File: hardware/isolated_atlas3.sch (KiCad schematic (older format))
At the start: 15 parts, among them J501 CONN_01X02, P5 ATLAS_DO_PROBE, U501 ADM3260, U502 ATLAS_DO

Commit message: Upgrade to Kicad 5.
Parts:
- C501, C502, C503, C504, C505, C506: symbol C -> fk-atlas-rescue:C
- J501: symbol CONN_01X02 -> fk-atlas-rescue:CONN_01X02
- P5: symbol WATER_PROBE -> fk-atlas-rescue:WATER_PROBE
- R501, R502, R503, R504, R505: symbol R -> fk-atlas-rescue:R
- U501: symbol adm3260 -> fk-atlas-rescue:adm3260
- U502: symbol ATLAS_SENSOR -> conservify:ATLAS_SENSOR
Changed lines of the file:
@@
-EESchema Schematic File Version 2
-LIBS:conservify
+EESchema Schematic File Version 4
 LIBS:fk-atlas-cache
-EELAYER 25 0
+EELAYER 26 0
 EELAYER END
 $Descr A4 11693 8268
@@
 $EndDescr
 $Comp
-L adm3260 U501
+L fk-atlas-rescue:adm3260 U501
 U 1 1 594C2CF0
 P 4400 2900
@@
 $EndComp
 $Comp
-L C C503
+L fk-atlas-rescue:C C503
 U 1 1 594C2CF5
 P 5650 3800
@@
 $EndComp
 $Comp
-L C C504
+L fk-atlas-rescue:C C504
 U 1 1 594C2CF9
 P 5650 4100
@@
 $EndComp
 $Comp
-L C C505
+L fk-atlas-rescue:C C505
 U 1 1 594C2CFC
 P 5650 4400
@@
 $EndComp
 $Comp
-L C C506
+L fk-atlas-rescue:C C506
 U 1 1 594C2D00
 P 5650 4650
@@
 $EndComp
 $Comp
-L C C501
+L fk-atlas-rescue:C C501
 U 1 1 5948D5F5
 P 2900 3800
@@
 $EndComp
 $Comp
-L C C502
+L fk-atlas-rescue:C C502
 U 1 1 5948D68D
 P 2900 4100
@@
 $EndComp
 $Comp
-L R R501
+L fk-atlas-rescue:R R501
 U 1 1 594C2D0D
 P 5650 3300
@@
 $EndComp
 $Comp
-L R R502
+L fk-atlas-rescue:R R502
 U 1 1 594C2D11
 P 6250 2700
@@
 $EndComp
 $Comp
-L R R504
+L fk-atlas-rescue:R R504
 U 1 1 594C2D15
 P 6700 2700
@@
 $EndComp
 $Comp
-L R R503
+L fk-atlas-rescue:R R503
 U 1 1 594C2D19
 P 6300 3250
@@
 $EndComp
 $Comp
-L R R505
+L fk-atlas-rescue:R R505
 U 1 1 594C2D1D
 P 6800 3250
@@
 $EndComp
 $Comp
-L VCC #PWR063
+L fk-atlas-rescue:VCC #PWR063
 U 1 1 5948EDC0
 P 2450 3750
@@
 $EndComp
 $Comp
-L VCC #PWR064
+L fk-atlas-rescue:VCC #PWR064
 U 1 1 5948EDF6
 P 2450 2350
@@
 $EndComp
 $Comp
-L ATLAS_SENSOR U502
+L conservify:ATLAS_SENSOR U502
 U 1 1 594C2D34
 P 8550 2900
@@
 $EndComp
 $Comp
-L CONN_01X02 J501
+L fk-atlas-rescue:CONN_01X02 J501
 U 1 1 594D403D
 P 10050 2950
@@
 $EndComp
 $Comp
-L WATER_PROBE P5
+L fk-atlas-rescue:WATER_PROBE P5
 U 1 1 59D2A6F4
 P 8800 3600

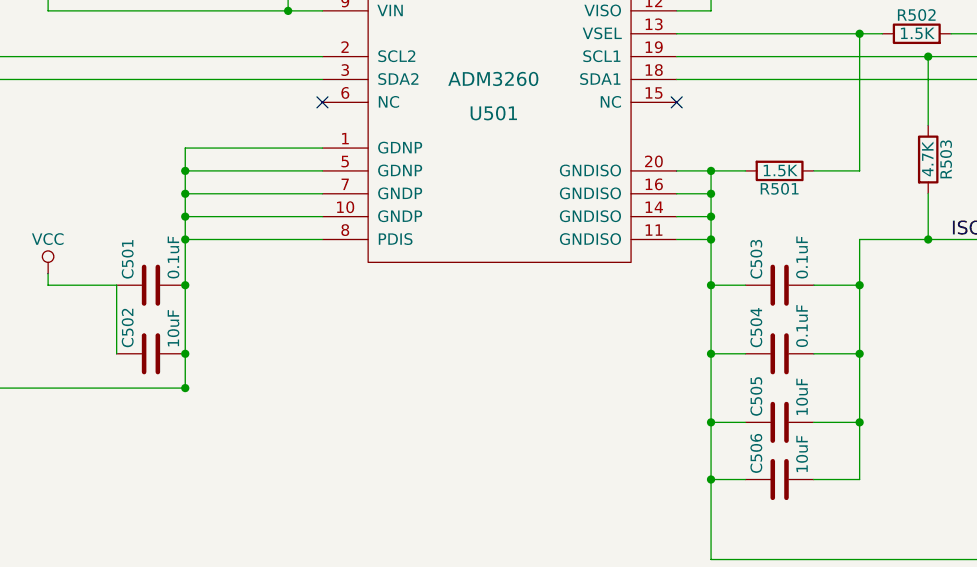
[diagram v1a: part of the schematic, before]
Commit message: Consistent part values across our schematics.
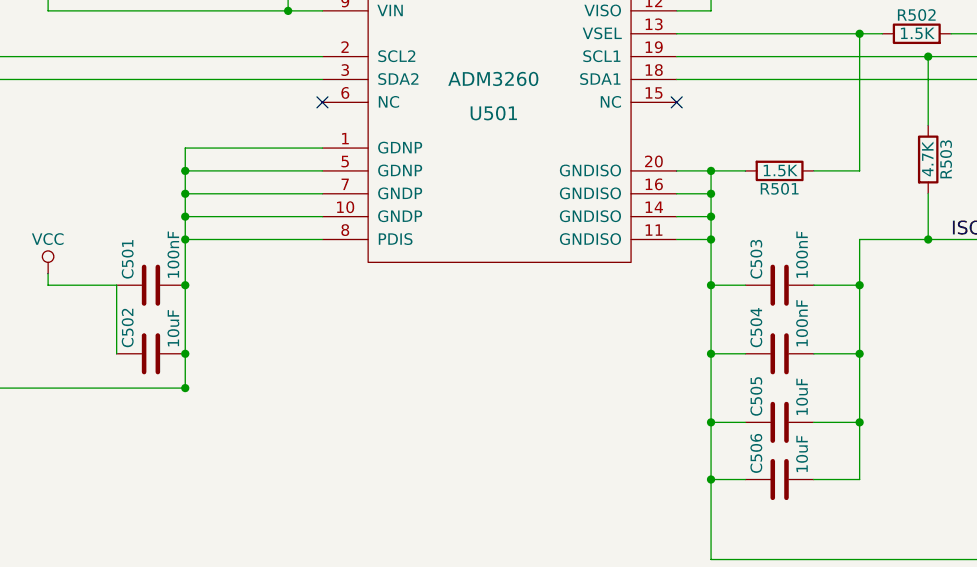
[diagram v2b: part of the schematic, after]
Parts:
- C501, C503, C504: value 0.1uF -> 100nF

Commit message: Part updates.
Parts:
- C501, C503, C504: Critical (none) -> (none); MFN (none) -> Murata Electronics; MFP (none) -> GRM188R71H104KA93D; Notes (none) -> (none); Package (none) -> (none); Source (none) -> ANY; Subsystem (none) -> (none); Supplier1 (none) -> mouser
- C502, C505, C506: Critical (none) -> (none); MFN (none) -> Taiyo Yuden; MFP (none) -> LMK107BBJ106KALT; Notes (none) -> (none); Package (none) -> (none); Source (none) -> ANY; Subsystem (none) -> (none); Supplier1 (none) -> mouser; spn1 81-GRM188R60J106ME47 -> 963-LMK107BBJ106KALT
- J501: Critical (none) -> (none); MFN (none) -> Amphenol RF; MFP (none) -> 031-5431; Notes (none) -> (none); Package (none) -> (none); Source (none) -> ANY; Subsystem (none) -> (none); Supplier1 (none) -> mouser
- P5: Critical (none) -> (none); MFN (none) -> (none); MFP (none) -> (none); Notes (none) -> (none); Package (none) -> (none); SPN1 (none) -> (none); Source (none) -> ANY; Subsystem (none) -> (none); Supplier1 (none) -> (none)
- R501, R502, R504: Critical (none) -> (none); MFN (none) -> (none); MFP (none) -> (none); Notes (none) -> (none); Package (none) -> (none); Source (none) -> ANY; Subsystem (none) -> (none); Supplier1 (none) -> (none)
- R503, R505: Critical (none) -> (none); MFN (none) -> Yageo; MFP (none) -> AF0603JR-074K7L; Notes (none) -> (none); Package (none) -> (none); Source (none) -> ANY; Subsystem (none) -> (none); Supplier1 (none) -> mouser
- U501: Critical (none) -> (none); MFN (none) -> Analog Devices / Linear Technology; MFP (none) -> ADM3260ARSZ; Notes (none) -> (none); Package (none) -> (none); Source (none) -> ANY; Subsystem (none) -> (none); Supplier1 (none) -> mouser
- U502: Critical (none) -> (none); MFN (none) -> (none); MFP (none) -> (none); Notes (none) -> (none); Package (none) -> (none); SPN1 (none) -> (none); Source (none) -> ANY; Subsystem (none) -> (none); Supplier1 (none) -> atlas

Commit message: Fix DRC in schematic mode.
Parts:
- C501, C502, C503, C504, C505, C506: symbol fk-atlas-rescue:C -> conservify:CAPACITOR_CERAMIC
- J501: symbol fk-atlas-rescue:CONN_01X02 -> conservify:CONN_01x02
- P5: symbol fk-atlas-rescue:WATER_PROBE -> conservify:ATLAS_WATER_PROBE
- R501, R502, R503, R504, R505: symbol fk-atlas-rescue:R -> conservify:R
- U501: symbol fk-atlas-rescue:adm3260 -> conservify:ADM3260
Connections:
- wire segments 52 -> 78
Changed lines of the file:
@@
 $EndDescr
 $Comp
-L fk-atlas-rescue:adm3260 U501
+L conservify:ADM3260 U501
 U 1 1 594C2CF0
 P 4400 2900
@@
 $EndComp
 $Comp
-L fk-atlas-rescue:C C503
+L conservify:CAPACITOR_CERAMIC C503
 U 1 1 594C2CF5
 P 5650 3800
@@
 $EndComp
 $Comp
-L fk-atlas-rescue:C C504
+L conservify:CAPACITOR_CERAMIC C504
 U 1 1 594C2CF9
 P 5650 4100
@@
 $EndComp
 $Comp
-L fk-atlas-rescue:C C505
+L conservify:CAPACITOR_CERAMIC C505
 U 1 1 594C2CFC
 P 5650 4400
@@
 $EndComp
 $Comp
-L fk-atlas-rescue:C C506
+L conservify:CAPACITOR_CERAMIC C506
 U 1 1 594C2D00
 P 5650 4650
@@
 $EndComp
 $Comp
-L fk-atlas-rescue:C C501
+L conservify:CAPACITOR_CERAMIC C501
 U 1 1 5948D5F5
 P 2900 3800
@@
 $EndComp
 $Comp
-L fk-atlas-rescue:C C502
+L conservify:CAPACITOR_CERAMIC C502
 U 1 1 5948D68D
 P 2900 4100
@@
 $EndComp
 $Comp
-L fk-atlas-rescue:R R501
+L conservify:R R501
 U 1 1 594C2D0D
 P 5650 3300
@@
 $EndComp
 $Comp
-L fk-atlas-rescue:R R502
+L conservify:R R502
 U 1 1 594C2D11
 P 6250 2700
@@
 $EndComp
 $Comp
-L fk-atlas-rescue:R R504
+L conservify:R R504
 U 1 1 594C2D15
 P 6700 2700
@@
 $EndComp
 $Comp
-L fk-atlas-rescue:R R503
+L conservify:R R503
 U 1 1 594C2D19
 P 6300 3250
@@
 $EndComp
 $Comp
-L fk-atlas-rescue:R R505
+L conservify:R R505
 U 1 1 594C2D1D
 P 6800 3250
@@
 $EndComp
 $Comp
-L fk-atlas-rescue:VCC #PWR063
+L conservify:VCC #PWR063
 U 1 1 5948EDC0
 P 2450 3750
@@
 $EndComp
 $Comp
-L fk-atlas-rescue:VCC #PWR064
+L conservify:VCC #PWR064
 U 1 1 5948EDF6
 P 2450 2350
@@
 $EndComp
 $Comp
-L fk-atlas-rescue:CONN_01X02 J501
+L conservify:CONN_01x02 J501
 U 1 1 594D403D
-P 10050 2950
-F 0 "J501" H 10050 3100 50  0000 C CNN
-F 1 "CONN_01X02" V 10150 2950 50  0000 C CNN
-F 2 "conservify:BNC" H 10050 2950 50  0001 C CNN
-F 3 "" H 10050 2950 50  0001 C CNN
-F 4 " " H 10050 3200 50  0001 C CNN "Critical"
-F 5 "Amphenol RF" H 10050 3200 50  0001 C CNN "MFN"
-F 6 "031-5431" H 10050 3200 50  0001 C CNN "MFP"
-F 7 " " H 10050 3200 50  0001 C CNN "Notes"
-F 8 " " H 10050 3200 50  0001 C CNN "Package"
-F 9 "ANY" H 10050 3200 50  0001 C CNN "Source"
-F 10 " " H 10050 3200 50  0001 C CNN "Subsystem"
-F 11 "mouser" H 10050 3200 50  0001 C CNN "Supplier1"
-F 12 "0" H 10050 3200 50  0001 C CNN "price"
-F 13 "523-31-5431" H 200 0   50  0001 C CNN "spn1"
-	1    10050 2950
-	1    0    0    -1
-$EndComp
-$Comp
-L fk-atlas-rescue:WATER_PROBE P5
+P 10050 2900
+F 0 "J501" H 10050 3050 50  0000 C CNN
+F 1 "CONN_01X02" V 10150 2900 50  0000 C CNN
+F 2 "conservify:BNC" H 10050 2900 50  0001 C CNN
+F 3 "" H 10050 2900 50  0001 C CNN
+F 4 " " H 10050 3150 50  0001 C CNN "Critical"
+F 5 "Amphenol RF" H 10050 3150 50  0001 C CNN "MFN"
+F 6 "031-5431" H 10050 3150 50  0001 C CNN "MFP"
+F 7 " " H 10050 3150 50  0001 C CNN "Notes"
+F 8 " " H 10050 3150 50  0001 C CNN "Package"
+F 9 "ANY" H 10050 3150 50  0001 C CNN "Source"
+F 10 " " H 10050 3150 50  0001 C CNN "Subsystem"
+F 11 "mouser" H 10050 3150 50  0001 C CNN "Supplier1"
+F 12 "0" H 10050 3150 50  0001 C CNN "price"
+F 13 "523-31-5431" H 200 -50 50  0001 C CNN "spn1"
+	1    10050 2900
+	1    0    0    -1
+$EndComp
+$Comp
+L conservify:ATLAS_WATER_PROBE P5
 U 1 1 59D2A6F4
 P 8800 3600
@@
 F 12 " " H 8800 3700 50  0001 C CNN "Supplier1"
 	1    8800 3600
+	1    0    0    -1
+$EndComp
+$Comp
+L conservify:PWR_FLAG #FLG0108
+U 1 1 5BCDA7BC
+P 7400 4900
+F 0 "#FLG0108" H 7400 4975 50  0001 C CNN
+F 1 "PWR_FLAG" H 7400 5050 50  0000 C CNN
+F 2 "" H 7400 4900 50  0001 C CNN
+F 3 "~" H 7400 4900 50  0001 C CNN
+	1    7400 4900
 	1    0    0    -1
 $EndComp
@@
 DO_PGND
 Wire Wire Line
-	5200 3300 5500 3300
-Wire Wire Line
-	5350 3300 5350 5000
+	5200 3300 5350 3300
+Wire Wire Line
+	5350 3300 5350 3400
 Wire Wire Line
 	5350 3600 5200 3600
@@
 	5800 3800 6000 3800
 Wire Wire Line
-	6000 3600 6000 4650
+	6000 3600 6000 3800
 Wire Wire Line
 	6000 4650 5800 4650
@@
 	5800 4100 6000 4100
 Wire Wire Line
-	5200 2800 7800 2800
-Wire Wire Line
-	5200 2900 7800 2900
-Wire Wire Line
-	5200 2700 6100 2700
+	5200 2800 6300 2800
+Wire Wire Line
+	5200 2900 6800 2900
+Wire Wire Line
+	5200 2700 6000 2700
 Wire Wire Line
 	6000 2700 6000 3300
@@
 	5350 2600 5350 2500
 Wire Wire Line
-	5200 2500 7400 2500
+	5200 2500 5350 2500
 Wire Wire Line
 	6900 2500 6900 2700
@@
 	6300 3400 6300 3600
 Wire Wire Line
-	6000 3600 6800 3600
+	6000 3600 6300 3600
 Wire Wire Line
 	6800 3600 6800 3400
 Wire Wire Line
-	2450 2600 3650 2600
-Wire Wire Line
-	2450 2350 2450 2600
+	2450 2600 3500 2600
+Wire Wire Line
+	2450 2350 2450 2450
 Wire Wire Line
 	3650 2500 3500 2500
@@
 	3650 3200 3050 3200
 Wire Wire Line
-	3050 3200 3050 4250
+	3050 3200 3050 3300
 Wire Wire Line
 	3050 4250 1750 4250
@@
 Wire Wire Line
 	9450 3000 9850 3000
+Wire Wire Line
+	7400 4900 7400 5000
+Wire Wire Line
+	5350 3500 5350 3600
+Wire Wire Line
+	5350 3400 5350 3500
+Wire Wire Line
+	5350 3600 5350 3800
+Wire Wire Line
+	5350 4400 5350 4650
+Wire Wire Line
+	5350 4100 5350 4400
+Wire Wire Line
+	5350 3800 5350 4100
+Wire Wire Line
+	6000 4400 6000 4650
+Wire Wire Line
+	6000 4100 6000 4400
+Wire Wire Line
+	5350 3300 5500 3300
+Wire Wire Line
+	5350 2500 6900 2500
+Wire Wire Line
+	6000 2700 6100 2700
+Wire Wire Line
+	6300 2800 7800 2800
+Wire Wire Line
+	6800 2900 7800 2900
+Wire Wire Line
+	3500 2600 3650 2600
+Wire Wire Line
+	3050 3800 3050 4100
+Wire Wire Line
+	3050 4100 3050 4250
+Wire Wire Line
+	3050 3600 3050 3800
+Wire Wire Line
+	3050 3500 3050 3600
+Wire Wire Line
+	3050 3400 3050 3500
+Wire Wire Line
+	3050 3300 3050 3400
+Wire Wire Line
+	2450 2450 2450 2600
+Wire Wire Line
+	5350 4650 5350 5000
+Wire Wire Line
+	6300 3600 6800 3600
+Wire Wire Line
+	6000 3800 6000 4100
+Wire Wire Line
+	6900 2500 7400 2500
 Connection ~ 5350 3500
 Connection ~ 5350 3400
@@
 Connection ~ 6300 3600
 Connection ~ 6000 3800
-Connection ~ 3050 4250
 Connection ~ 6900 2500
 NoConn ~ 3650 3000

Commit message: Drop prototype Atlas modules - focus on getting OEM boards working.
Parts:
- U502: footprint conservify:ATLAS_SENSOR_BOARD_COMBO -> conservify:ATLAS_SENSOR_BOARD_OEM
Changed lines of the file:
@@
 F 0 "U502" H 8100 2550 60  0000 C CNN
 F 1 "ATLAS_DO" H 8600 2850 60  0000 C CNN
-F 2 "conservify:ATLAS_SENSOR_BOARD_COMBO" H 8550 2900 60  0001 C CNN
+F 2 "conservify:ATLAS_SENSOR_BOARD_OEM" H 8550 2900 60  0001 C CNN
 F 3 "" H 8550 2900 60  0001 C CNN
 F 4 " " H 8100 2650 50  0001 C CNN "Critical"
